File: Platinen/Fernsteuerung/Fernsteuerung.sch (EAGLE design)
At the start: 7 parts, among them K1 ESP32DEVKITV11000MIL, P1 TFT_3.5"_SPI_480X320, U1 COM-09032

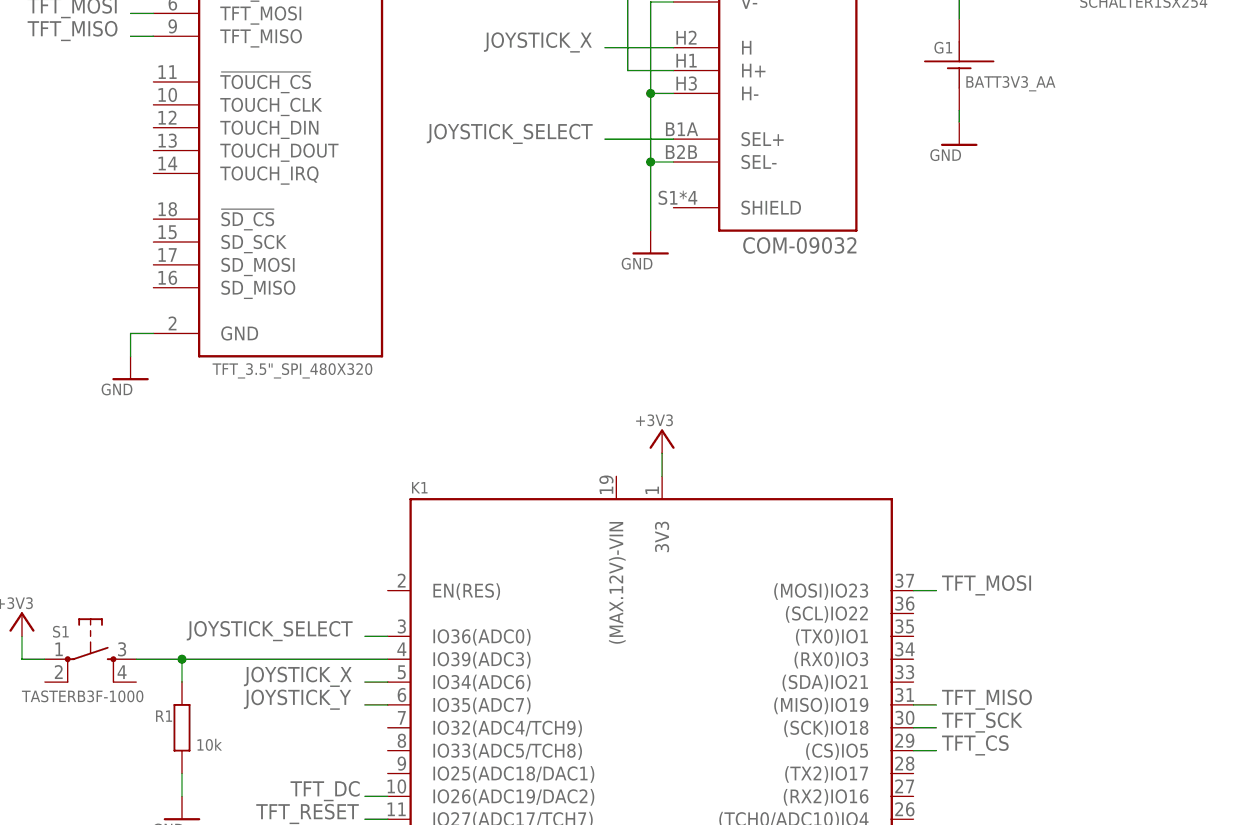
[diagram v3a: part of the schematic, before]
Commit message: Fernsteuerung Plaine fertig
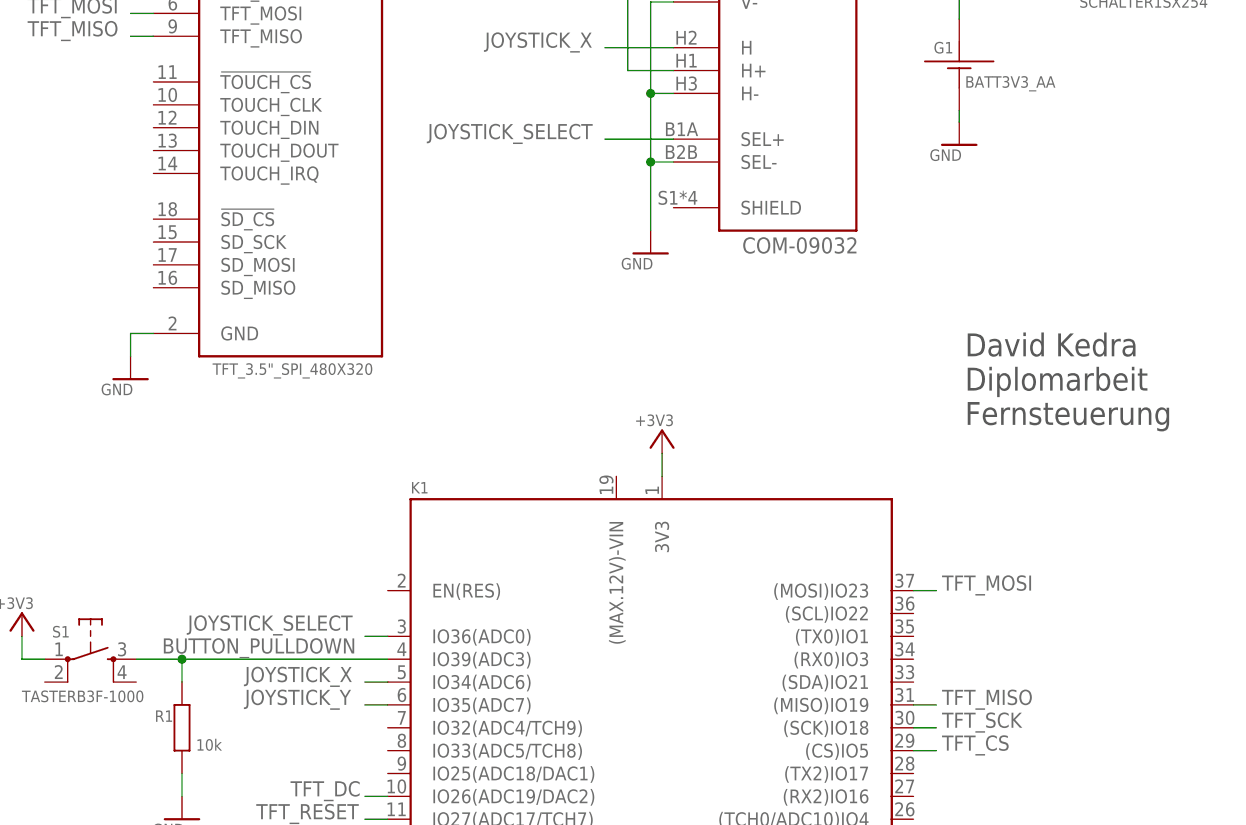
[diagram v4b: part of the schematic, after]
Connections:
- net N$1 renamed BUTTON_PULLDOWN
- net N$2 renamed BATTERY_+3V3
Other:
- note added: "David Kedra Diplomarbeit Fernsteuerung"
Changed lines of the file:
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@@
 <setting verticaltext="up"/>
 </settings>
-<grid distance="25" unitdist="mil" unit="mil" style="lines" multiple="1" display="no" altdistance="0.01" altunitdist="inch" altunit="inch"/>
+<grid distance="0.1" unitdist="inch" unit="inch" style="lines" multiple="1" display="no" altdistance="0.01" altunitdist="inch" altunit="inch"/>
 <layers>
 <layer number="1" name="Top" color="4" fill="1" visible="no" active="no"/>
@@
 <sheet>
 <plain>
+<text x="114.3" y="88.9" size="2.54" layer="97">David Kedra
+Diplomarbeit
+Fernsteuerung</text>
 </plain>
 <instances>
@@
 <net name="GND" class="0">
 <segment>
-<pinref part="U1" gate="G$1" pin="V-"/>
-<wire x1="81.915" y1="135.89" x2="79.375" y2="135.89" width="0.1524" layer="91"/>
-<wire x1="79.375" y1="135.89" x2="79.375" y2="125.73" width="0.1524" layer="91"/>
-<pinref part="U1" gate="G$1" pin="H-"/>
-<wire x1="79.375" y1="125.73" x2="81.915" y2="125.73" width="0.1524" layer="91"/>
-<wire x1="79.375" y1="125.73" x2="79.375" y2="118.11" width="0.1524" layer="91"/>
-<junction x="79.375" y="125.73"/>
-<pinref part="U1" gate="G$1" pin="SEL-"/>
-<wire x1="79.375" y1="118.11" x2="81.915" y2="118.11" width="0.1524" layer="91"/>
-<wire x1="79.375" y1="118.11" x2="79.375" y2="110.49" width="0.1524" layer="91"/>
-<junction x="79.375" y="118.11"/>
-<pinref part="GND1" gate="1" pin="GND"/>
-</segment>
-<segment>
 <pinref part="GND2" gate="1" pin="GND"/>
 <pinref part="K1" gate="G$1" pin="GND"/>
@@
 <pinref part="GND5" gate="1" pin="GND"/>
 </segment>
+<segment>
+<pinref part="U1" gate="G$1" pin="V-"/>
+<wire x1="81.915" y1="135.89" x2="79.375" y2="135.89" width="0.1524" layer="91"/>
+<wire x1="79.375" y1="135.89" x2="79.375" y2="125.73" width="0.1524" layer="91"/>
+<pinref part="U1" gate="G$1" pin="H-"/>
+<wire x1="79.375" y1="125.73" x2="81.915" y2="125.73" width="0.1524" layer="91"/>
+<wire x1="79.375" y1="125.73" x2="79.375" y2="118.11" width="0.1524" layer="91"/>
+<junction x="79.375" y="125.73"/>
+<pinref part="U1" gate="G$1" pin="SEL-"/>
+<wire x1="79.375" y1="118.11" x2="81.915" y2="118.11" width="0.1524" layer="91"/>
+<pinref part="GND1" gate="1" pin="GND"/>
+<wire x1="79.375" y1="110.49" x2="79.375" y2="118.11" width="0.1524" layer="91"/>
+<junction x="79.375" y="118.11"/>
+</segment>
 </net>
 <net name="JOYSTICK_SELECT" class="0">
@@
 <pinref part="K1" gate="G$1" pin="IO36(ADC0)"/>
 <wire x1="47.625" y1="65.405" x2="50.165" y2="65.405" width="0.1524" layer="91"/>
-<label x="27.94" y="65.405" size="1.6764" layer="95"/>
+<label x="27.94" y="66.04" size="1.6764" layer="95"/>
 </segment>
 </net>
@@
 </segment>
 </net>
-<net name="N$1" class="0">
+<net name="BUTTON_PULLDOWN" class="0">
 <segment>
 <pinref part="K1" gate="G$1" pin="IO39(ADC3)"/>
@@
 <wire x1="27.305" y1="62.865" x2="27.305" y2="60.325" width="0.1524" layer="91"/>
 <junction x="27.305" y="62.865"/>
-</segment>
-</net>
-<net name="N$2" class="0">
+<label x="25.0825" y="63.5" size="1.6764" layer="95"/>
+</segment>
+</net>
+<net name="BATTERY_+3V3" class="0">
 <segment>
 <pinref part="G1" gate="G$1" pin="PLUS"/>
